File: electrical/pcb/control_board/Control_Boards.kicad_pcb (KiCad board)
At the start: 2 copper layers, 181.6 x 252.8 mm, 118 parts, among them J1 XT30-M, J10 Molex_172675-0613, J11 Molex_172675-0613, J12 TSW-104-07-F-T, J13 Molex_172675-0613, J14 Molex_172675-0613, J15 TSW-104-07-F-T, J16 277-11404-ND, J17 277-11404-ND, J18 277-11404-ND, J19 TSW-104-07-F-T, J2 XT30-F, J20 PEC08SAAN, J21 PPTC102LFBN-RC, J22 S9175-ND_rpi_breakout, J23 S9175-ND_rpi_breakout, J24 6posheader, J25 SSW-104-01-F-T, J26 WM6548-ND, J27 PPTC021LFBN-RC, J28 PPTC021LFBN-RC, J29 PPTC021LFBN-RC, J3 XT30-F, J4 XT30-F, J5 XT30-M, J6 ED2580-ND, J7 TSW-104-07-F-T, J8 Molex_172675-0613, J9 Molex_172675-0613, M1 Mounting_Holes, Q1 2N3906, Q2 2N3906, Q3 2N3906, SW1 CT206124-ND, T1 test_point, T2 test_point, T3 test_point, T4 test_point, T5 test_point, U1 INA260, U2 PCA9685, U3 D24V22Fx, U4 D24V150Fx, U5 DC7G3HWA, U6 DC7G3HWA, y1 rover_silkscreen

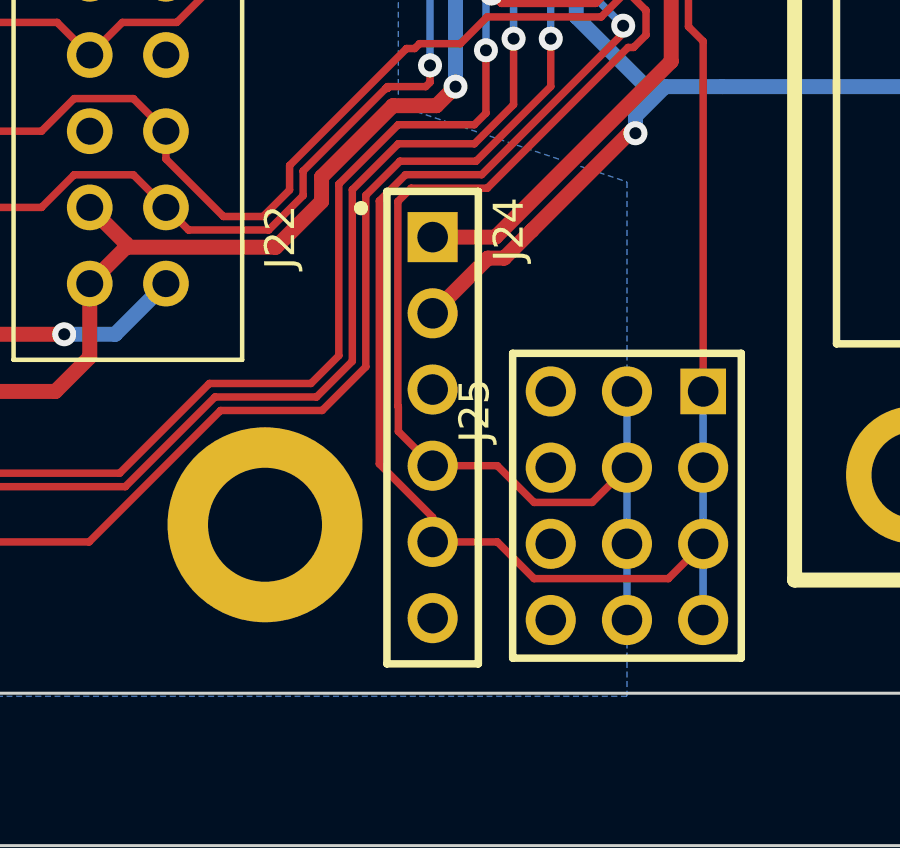
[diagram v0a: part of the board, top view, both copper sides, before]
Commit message: Fixing footprint for 455-1708-ND and updating in the layout
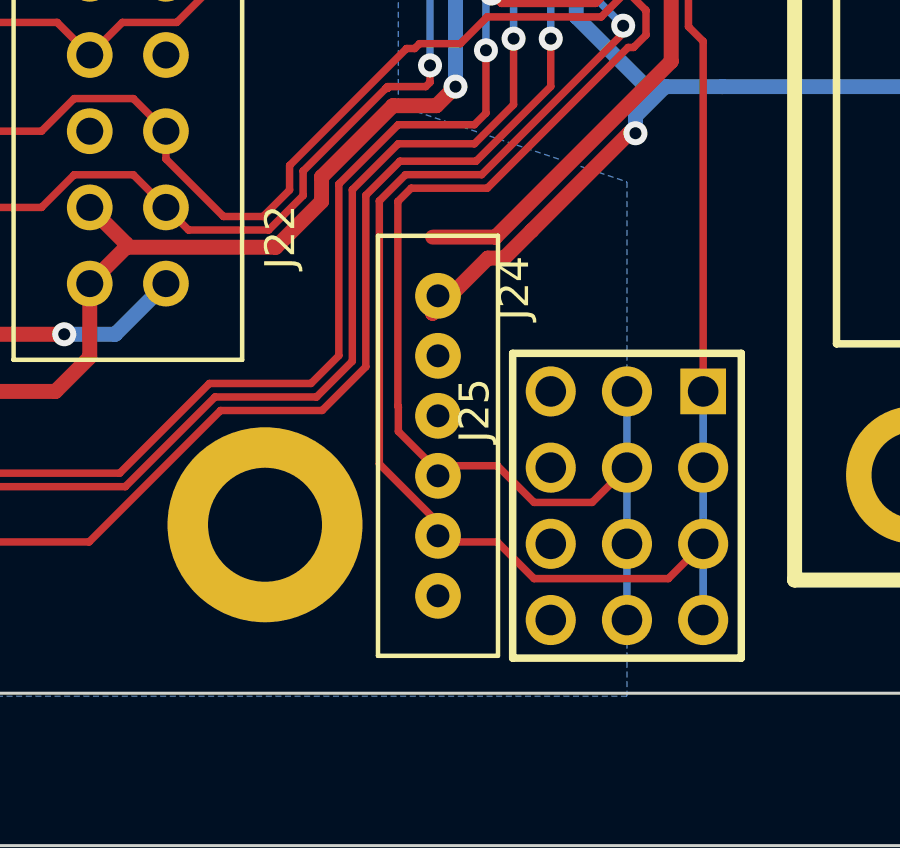
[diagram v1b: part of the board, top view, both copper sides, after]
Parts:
- moved J24 1.96 mm to (25.5, -174.6)

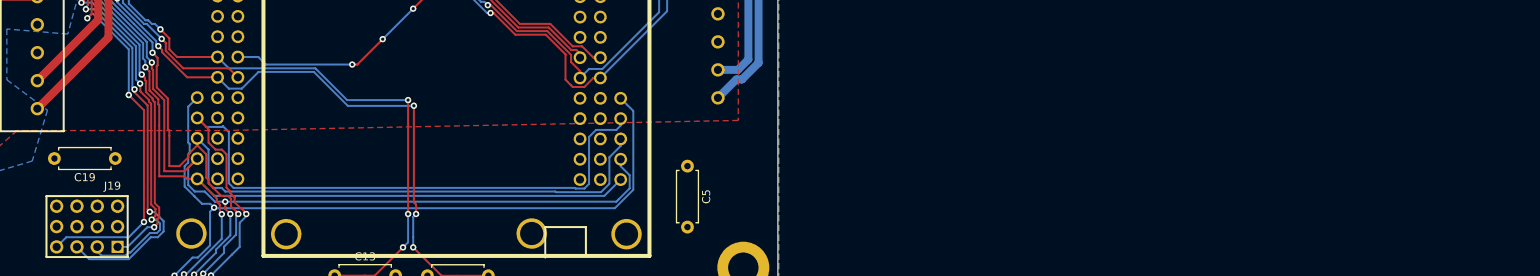
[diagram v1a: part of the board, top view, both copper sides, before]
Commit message: Touching up 3d models for j24, LED arrays, c19
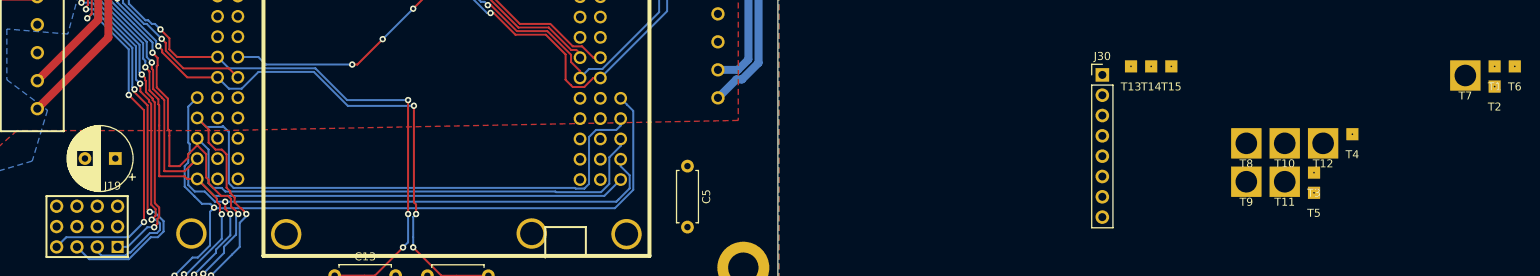
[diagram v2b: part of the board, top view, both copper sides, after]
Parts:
- added J30: PEC08SAAN, Connector_PinHeader_2.54mm:PinHeader_1x08_P2.54mm_Vertical, F.Cu at (222.0, -28.5)
- added T1: test_point, JPL Robotics:test_point, F.Cu at (271.1, -29.6)
- added T10: test_point, JPL Robotics:test_point_hole, F.Cu at (244.9, -20.0)
- added T11: test_point, JPL Robotics:test_point_hole, F.Cu at (244.9, -15.2)
- added T12: test_point, JPL Robotics:test_point_hole, F.Cu at (249.7, -20.0)
- added T13: test_point, JPL Robotics:test_point, F.Cu at (225.6, -29.6)
- added T14: test_point, JPL Robotics:test_point, F.Cu at (228.2, -29.6)
- added T15: test_point, JPL Robotics:test_point, F.Cu at (230.7, -29.6)
- added T2: test_point, JPL Robotics:test_point, F.Cu at (271.1, -27.1)
- added T3: test_point, JPL Robotics:test_point, F.Cu at (248.5, -16.3)
- added T4: test_point, JPL Robotics:test_point, F.Cu at (253.3, -21.1)
- added T5: test_point, JPL Robotics:test_point, F.Cu at (248.5, -13.8)
- added T6: test_point, JPL Robotics:test_point, F.Cu at (273.6, -29.6)
- added T7: test_point, JPL Robotics:test_point_hole, F.Cu at (267.4, -28.5)
- added T8: test_point, JPL Robotics:test_point_hole, F.Cu at (240.1, -20.0)
- added T9: test_point, JPL Robotics:test_point_hole, F.Cu at (240.1, -15.2)
- C19: footprint Resistor_THT:R_Axial_DIN0207_L6.3mm_D2.5mm_P7.62mm_Horizontal -> Capacitor_THT:CP_Radial_D8.0mm_P3.80mm
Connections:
- C19 pad 1: GND_motor -> +5V_motor
- C19 pad 2: +5V_motor -> GND_motor
- J20 pad 1: +5V_motor -> GND_motor
- J20 pad 2: +12V_motor -> +3.3V_motor
- J20 pad 3: GND_motor -> +5V_motor
- J20 pad 4: /Motor Board/TXD -> +12V_motor
- J20 pad 5: /Motor Board/RXD -> /Motor Board/TXD
- J20 pad 6: /Motor Board/SCL_rpi -> /Motor Board/RXD
- J20 pad 7: /Motor Board/SDA_rpi -> /Motor Board/SCL_rpi
- J20 pad 8: Net-(J20-Pad8) -> /Motor Board/SDA_rpi
- J22 pad 11: Net-(J22-Pad11) -> /Brain Board/X_RPI_GPIO_GEN0
- J22 pad 12: Net-(J22-Pad12) -> /Brain Board/X_RPI_GPIO_GEN1
- J22 pad 19: Net-(J22-Pad19) -> /Brain Board/X_RPI_SPI_MOSI
- J22 pad 21: Net-(J22-Pad21) -> /Brain Board/X_RPI_SPI_MISO
- J22 pad 23: Net-(J22-Pad23) -> /Brain Board/X_RPI_SPI_CLK
- J22 pad 24: Net-(J22-Pad24) -> /Brain Board/X_RPI_SPI_CE0_N
- J22 pad 26: Net-(J22-Pad26) -> /Brain Board/X_RPI_SPI_CE1_N
- J22 pad 27: Net-(J22-Pad27) -> /Brain Board/X_RPI_EEPROM_IDSD
- J22 pad 28: Net-(J22-Pad28) -> /Brain Board/X_RPI_EEPROM_IDSC
- J22 pad 32: Net-(J22-Pad32) -> /Brain Board/X_RPI_GPIO12
- J22 pad 33: Net-(J22-Pad33) -> /Brain Board/X_RPI_GPIO13
- J22 pad 35: Net-(J22-Pad35) -> /Brain Board/X_RPI_GPIO19
- J22 pad 36: Net-(J22-Pad36) -> /Brain Board/X_RPI_GPIO16
- J22 pad 38: Net-(J22-Pad38) -> /Brain Board/X_RPI_GPIO20
- J22 pad 40: Net-(J22-Pad40) -> /Brain Board/X_RPI_GPIO21
- J22 pad 7: Net-(J22-Pad7) -> /Brain Board/X_RPI_GPIO_GCLK
- J23 pad 11: Net-(J23-Pad11) -> /Brain Board/X_RPI_GPIO_GEN0
- J23 pad 12: Net-(J23-Pad12) -> /Brain Board/X_RPI_GPIO_GEN1
- J23 pad 13: Net-(J23-Pad13) -> /Brain Board/alert
- J23 pad 15: Net-(J23-Pad15) -> /Brain Board/OEservos
- J23 pad 16: Net-(J23-Pad16) -> /Brain Board/E_STOP_pi
- J23 pad 18: Net-(J23-Pad18) -> /Brain Board/12V_EN
- J23 pad 19: Net-(J23-Pad19) -> /Brain Board/X_RPI_SPI_MOSI
- J23 pad 21: Net-(J23-Pad21) -> /Brain Board/X_RPI_SPI_MISO
- J23 pad 22: Net-(J23-Pad22) -> /Brain Board/RPI_LED_1
- J23 pad 23: Net-(J23-Pad23) -> /Brain Board/X_RPI_SPI_CLK
- J23 pad 24: Net-(J23-Pad24) -> /Brain Board/X_RPI_SPI_CE0_N
- J23 pad 26: Net-(J23-Pad26) -> /Brain Board/X_RPI_SPI_CE1_N
- J23 pad 27: Net-(J23-Pad27) -> /Brain Board/X_RPI_EEPROM_IDSD
- J23 pad 28: Net-(J23-Pad28) -> /Brain Board/X_RPI_EEPROM_IDSC
- J23 pad 29: Net-(J23-Pad29) -> /Brain Board/RPI_LED_3
- J23 pad 31: Net-(J23-Pad31) -> /Brain Board/RPI_LED_4
- J23 pad 32: Net-(J23-Pad32) -> /Brain Board/X_RPI_GPIO12
- J23 pad 33: Net-(J23-Pad33) -> /Brain Board/X_RPI_GPIO13
- J23 pad 35: Net-(J23-Pad35) -> /Brain Board/X_RPI_GPIO19
- J23 pad 36: Net-(J23-Pad36) -> /Brain Board/X_RPI_GPIO16
- J23 pad 37: Net-(J23-Pad37) -> /Brain Board/RPI_LED_2
- J23 pad 38: Net-(J23-Pad38) -> /Brain Board/X_RPI_GPIO20
- J23 pad 40: Net-(J23-Pad40) -> /Brain Board/X_RPI_GPIO21
- J23 pad 7: Net-(J23-Pad7) -> /Brain Board/X_RPI_GPIO_GCLK

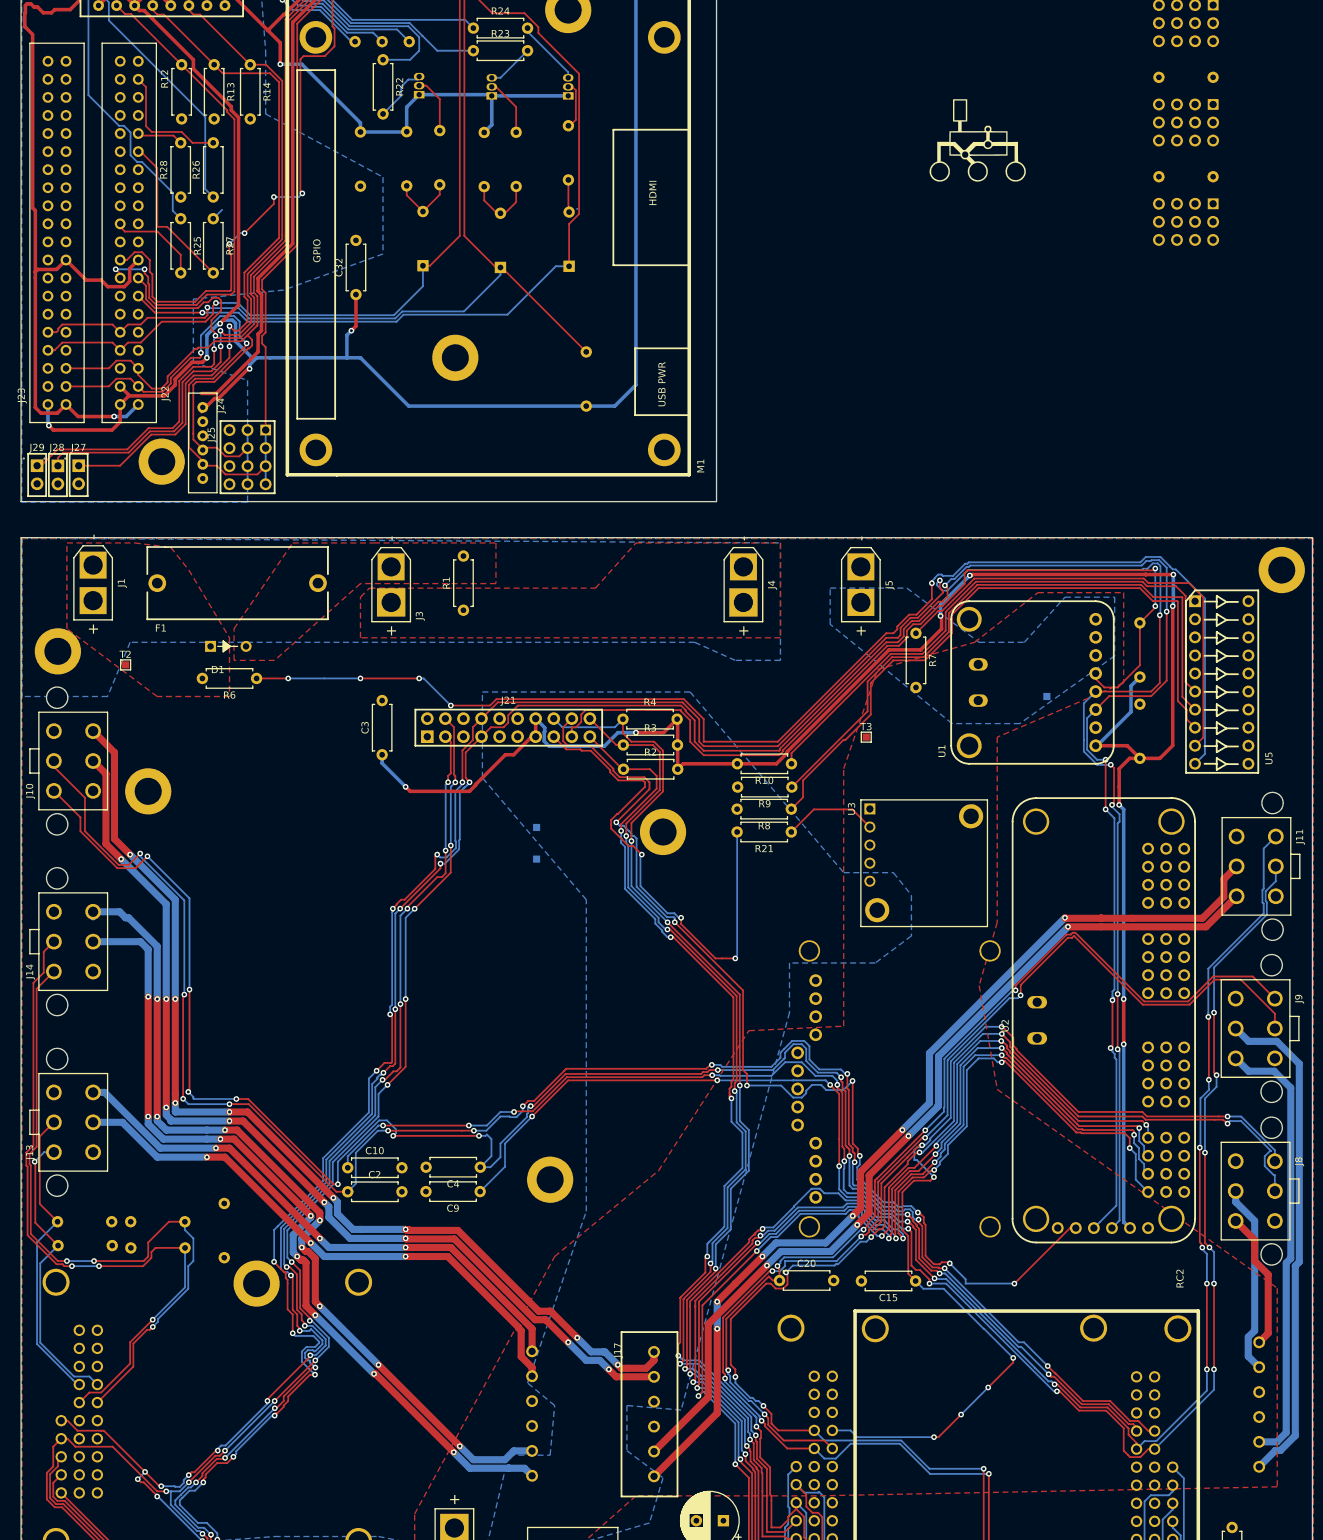
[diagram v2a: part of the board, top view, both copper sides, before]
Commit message: Updated footprint for rpi breakout connectors to indicate direction, rotated roboclaw motor channel output connectors by 180 degrees
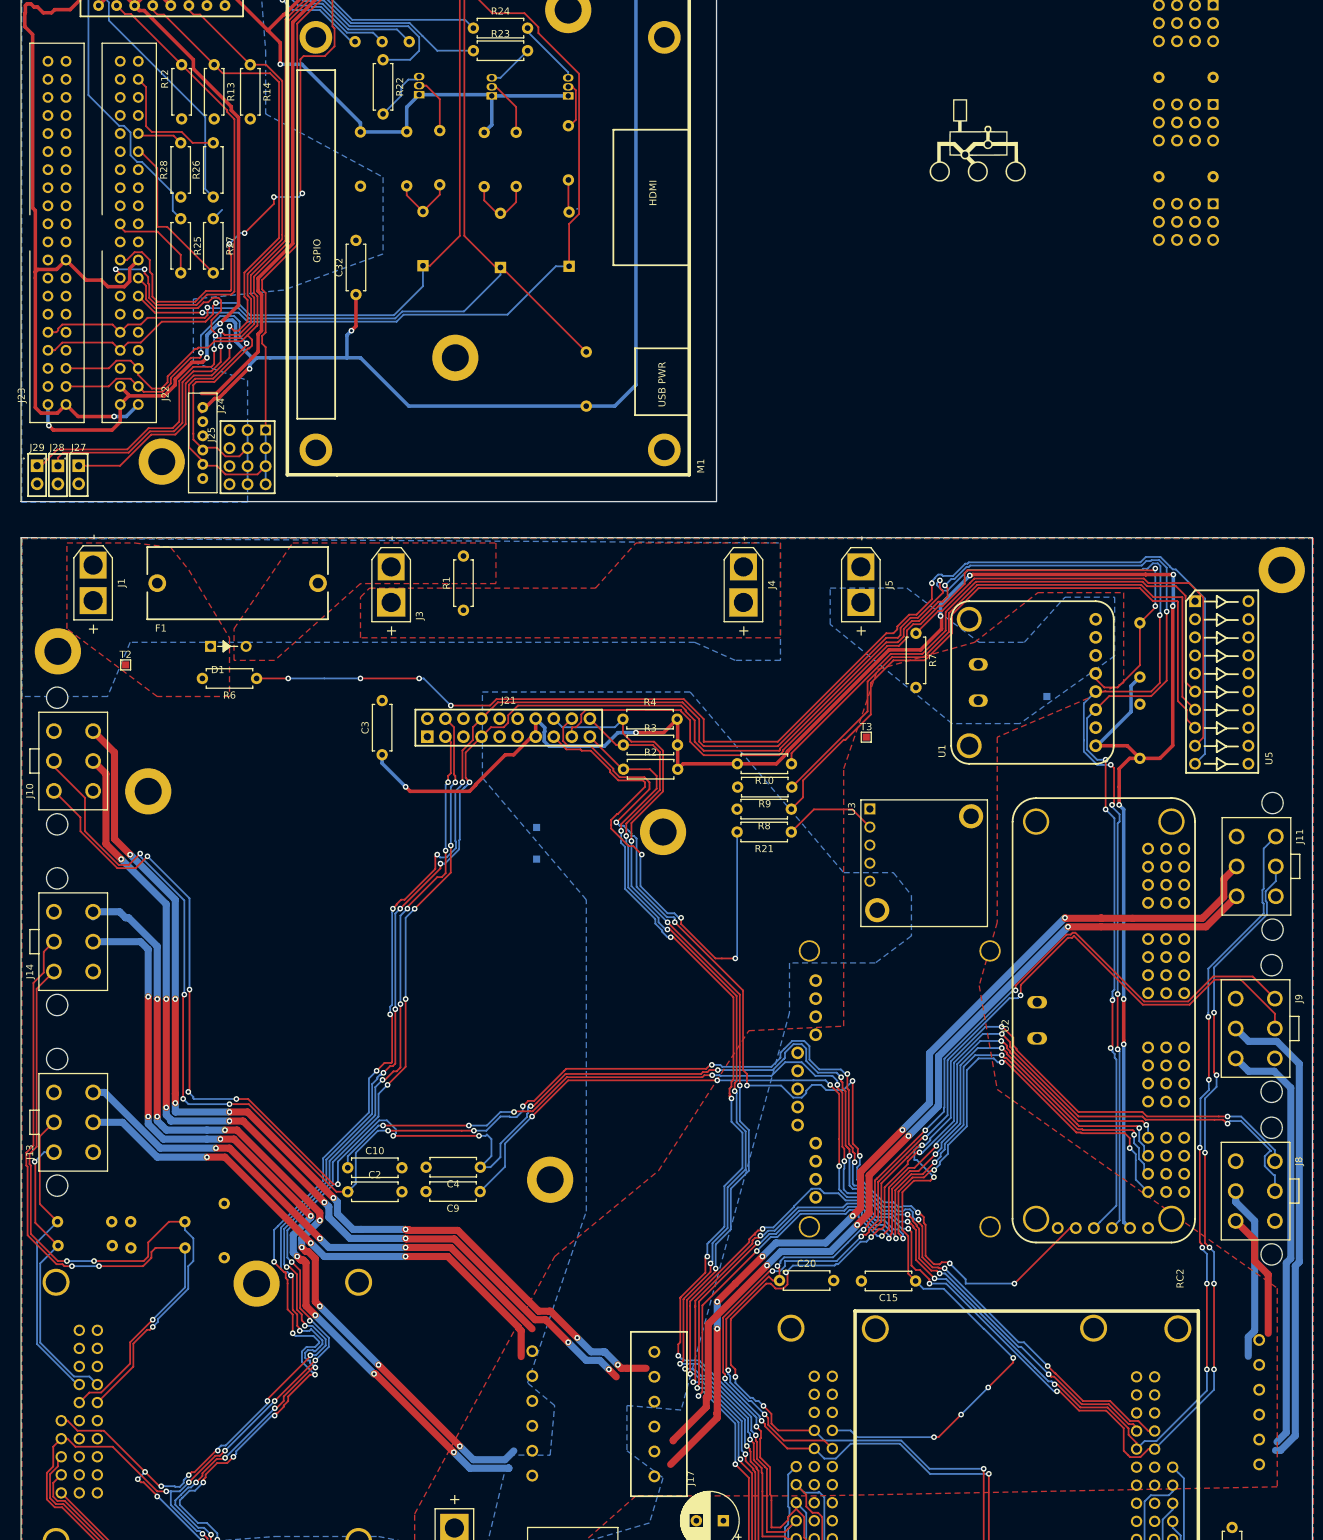
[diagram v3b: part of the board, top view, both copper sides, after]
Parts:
- moved J17 17.5 mm to (89.0, -24.3), turned to 90 degrees
- moved J18 17.5 mm to (71.8, -24.4), turned to 90 degrees
- moved J16 17.2 mm to (174.0, -26.0), turned to 90 degrees
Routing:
- net /Motor Board/RC2M1B: track 138.9 -> 133.5 mm
- net /Motor Board/RC3M2B: track 117.3 -> 113.6 mm
- net /Motor Board/RC3M1B: track 79.4 -> 76.0 mm
- net /Motor Board/RC1M2B: track 70.4 -> 67.2 mm
- net /Motor Board/RC3M1A: track 78.7 -> 75.5 mm
- net /Motor Board/RC2M1A: track 143.2 -> 140.5 mm
- net /Motor Board/RC3M2A: track 119.2 -> 116.7 mm
- net /Motor Board/RC2M2B: track 135.3 -> 132.8 mm
- net /Motor Board/RC1M2A: track 62.6 -> 60.0 mm
- net /Motor Board/RC2M2A: track 127.5 -> 125.0 mm
- net /Motor Board/RC1M1B: track 26.9 -> 24.7 mm
- net /Motor Board/RC1M1A: track 19.5 -> 17.7 mm

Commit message: Adding some pin number hints to footprint silkscreens
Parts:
- added ?: , , F.Cu at (219.5, -7.57)
- added ?: , , F.Cu at (225.0, -3.40)
- added ?: , , F.Cu at (46.3, -11.7)
- added ?: , , F.Cu at (28.6, -11.7)
- moved J30 32.6 mm to (201.7, -3.05), turned to 90 degrees

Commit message: Fix orientation of j2
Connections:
- J2 pad 1: +BATT -> GND_motor
- J2 pad 2: GND_motor -> +BATT
